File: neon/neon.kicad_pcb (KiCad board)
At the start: 2 copper layers, 60 x 50 mm, 32 parts, among them J1 V3V3-VIO, J2 3xV3V3-GND, J5 VBUS-VCC, U1 FT4232H_module, U2 C, U3 B, U4 A, U5 D, U6 74HC595

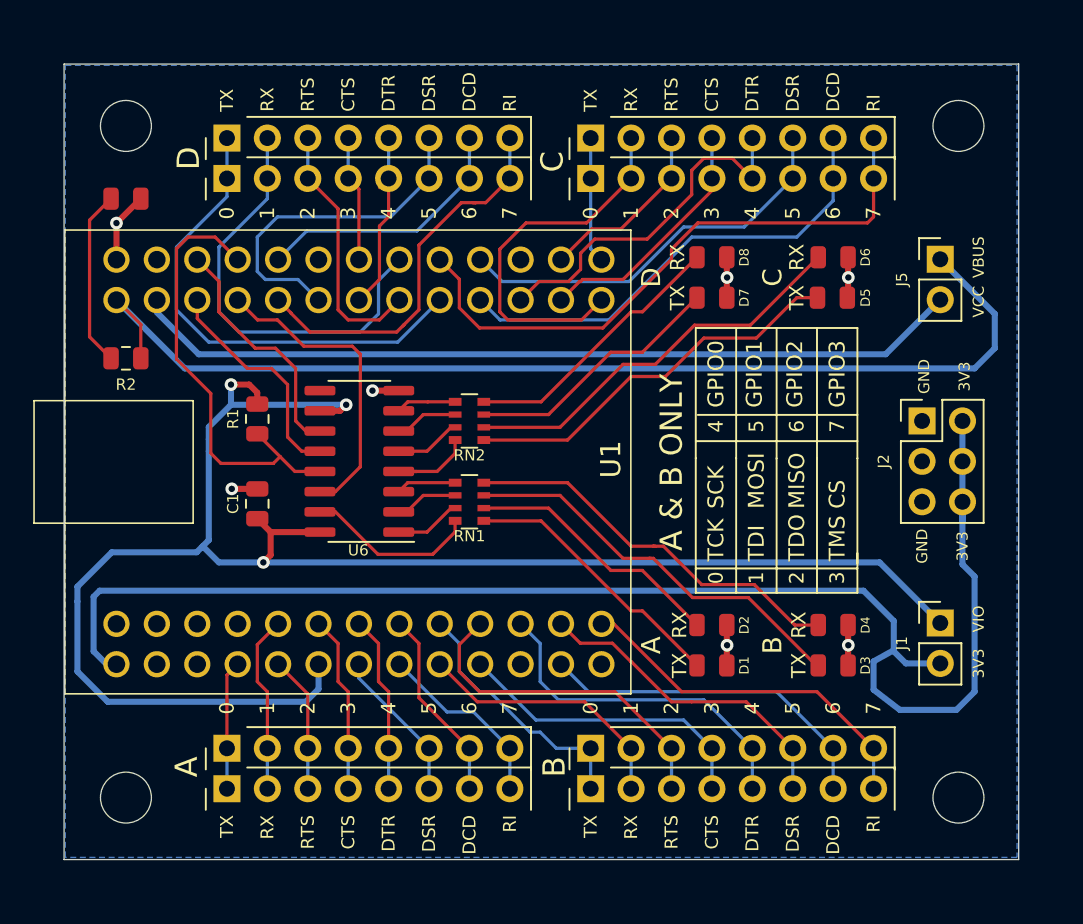
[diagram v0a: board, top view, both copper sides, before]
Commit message: Minor modifications following data review
Updated with updated copper pour, rounded edges. descrete resistors
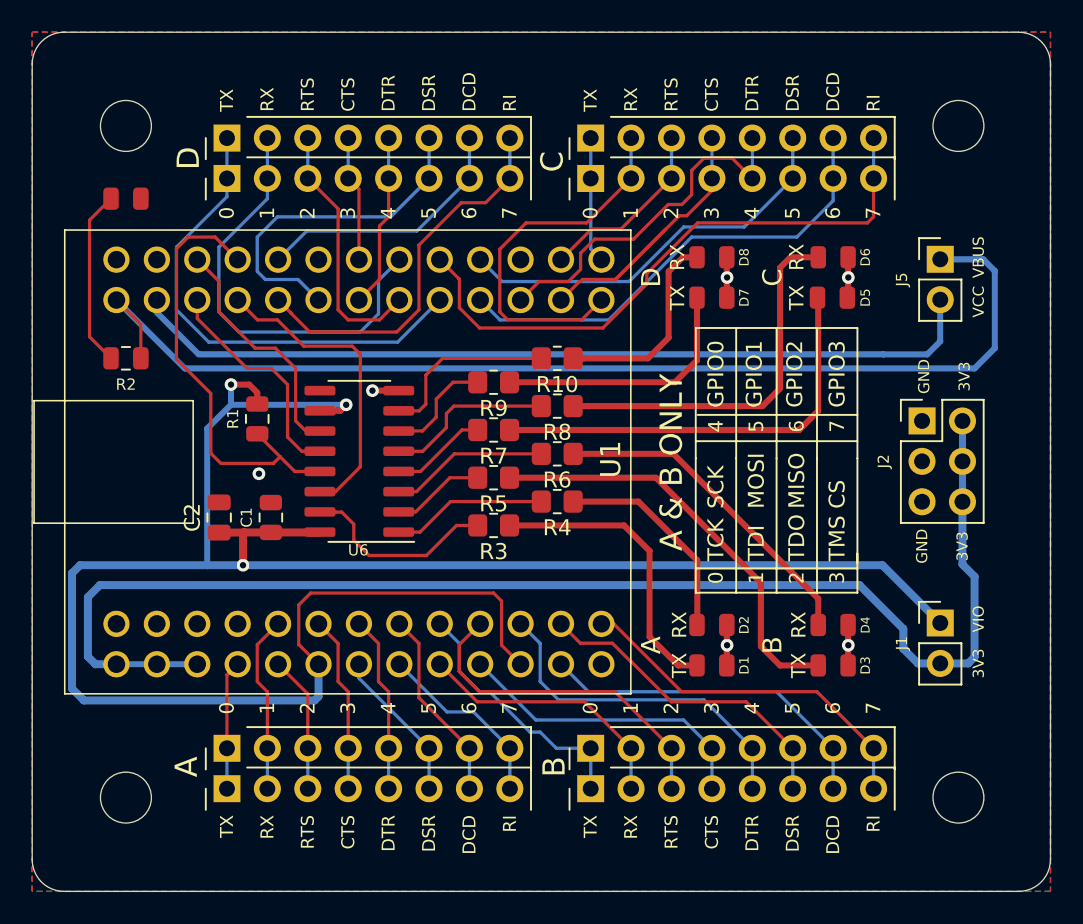
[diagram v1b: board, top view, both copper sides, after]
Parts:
- removed RN1, RN2: 330, Resistor_SMD:R_Array_Convex_4x0603
- added C2: 1uF, Capacitor_SMD:C_0805_2012Metric, F.Cu at (125.2, 108.4)
- added G***: LOGO, neon_footprints:sdg30pcbnew, B.Cu at (159.2, 104.9)
- added R10: 300R, Resistor_SMD:R_0805_2012Metric_Pad1.20x1.40mm_HandSolder, F.Cu at (146.5, 98.4)
- added R3: 300R, Resistor_SMD:R_0805_2012Metric_Pad1.20x1.40mm_HandSolder, F.Cu at (142.5, 108.9)
- added R4: 300R, Resistor_SMD:R_0805_2012Metric_Pad1.20x1.40mm_HandSolder, F.Cu at (146.5, 107.4)
- added R5: 300R, Resistor_SMD:R_0805_2012Metric_Pad1.20x1.40mm_HandSolder, F.Cu at (142.5, 105.9)
- added R6: 300R, Resistor_SMD:R_0805_2012Metric_Pad1.20x1.40mm_HandSolder, F.Cu at (146.5, 104.4)
- added R7: 300R, Resistor_SMD:R_0805_2012Metric_Pad1.20x1.40mm_HandSolder, F.Cu at (142.5, 102.9)
- added R8: 300R, Resistor_SMD:R_0805_2012Metric_Pad1.20x1.40mm_HandSolder, F.Cu at (146.5, 101.4)
- added R9: 300R, Resistor_SMD:R_0805_2012Metric_Pad1.20x1.40mm_HandSolder, F.Cu at (142.5, 99.9)
- R2: value 100 -> 300R
- moved G*** 15.4 mm to (143.2, 104.9)
- moved C1 1.21 mm to (128.5, 108.4)
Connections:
- net /FT4232H.sch/AD0 renamed /AD0
- net /FT4232H.sch/AD1 renamed /AD1
- net /FT4232H.sch/AD2 renamed /AD2
- net /FT4232H.sch/AD3 renamed /AD3
- net /FT4232H.sch/AD4 renamed /AD4
- net /FT4232H.sch/AD5 renamed /AD5
- net /FT4232H.sch/AD6 renamed /AD6
- net /FT4232H.sch/AD7 renamed /AD7
- net /FT4232H.sch/BD0 renamed /BD0
- net /FT4232H.sch/BD1 renamed /BD1
- net /FT4232H.sch/BD2 renamed /BD2
- net /FT4232H.sch/BD3 renamed /BD3
- net /FT4232H.sch/BD4 renamed /BD4
- net /FT4232H.sch/BD5 renamed /BD5
- net /FT4232H.sch/BD6 renamed /BD6
- net /FT4232H.sch/BD7 renamed /BD7
- net /FT4232H.sch/CD0 renamed /CD0
- net /FT4232H.sch/CD1 renamed /CD1
- net /FT4232H.sch/CD2 renamed /CD2
- net /FT4232H.sch/CD3 renamed /CD3
- net /FT4232H.sch/CD4 renamed /CD4
- net /FT4232H.sch/CD5 renamed /CD5
- net /FT4232H.sch/CD6 renamed /CD6
- net /FT4232H.sch/CD7 renamed /CD7
- net /FT4232H.sch/CLK renamed /CLK
- net /FT4232H.sch/CS renamed /CS
- net /FT4232H.sch/DATA renamed /DATA
- net /FT4232H.sch/DD0 renamed /DD0
- net /FT4232H.sch/DD1 renamed /DD1
- net /FT4232H.sch/DD2 renamed /DD2
- net /FT4232H.sch/DD3 renamed /DD3
- net /FT4232H.sch/DD4 renamed /DD4
- net /FT4232H.sch/DD5 renamed /DD5
- net /FT4232H.sch/DD6 renamed /DD6
- net /FT4232H.sch/DD7 renamed /DD7
- net /FT4232H.sch/PWREN renamed /PWREN
- net /FT4232H.sch/VBUS renamed /VBUS
- net /FT4232H.sch/VCC renamed /VCC
- C1 pad 1: /FT4232H.sch/VIO -> /VIO
- J1 pad 1: /FT4232H.sch/VIO -> /VIO
- R1 pad 2: /FT4232H.sch/VIO -> /VIO
- U1 pad 11: (no net) -> /VIO
- U1 pad 13: (no net) -> no_connect_59
- U1 pad 14: (no net) -> GND
- U1 pad 15: (no net) -> GND
- U1 pad 16: (no net) -> GND
- U1 pad 17: (no net) -> no_connect_60
- U1 pad 2: (no net) -> V3V3
- U1 pad 3: (no net) -> V3V3
- U1 pad 41: (no net) -> GND
- U1 pad 45: (no net) -> no_connect_61
- U1 pad 50: (no net) -> no_connect_62
- U1 pad 6: /FT4232H.sch/VIO -> /VIO
- U6 pad 10: /FT4232H.sch/VIO -> /VIO
- U6 pad 16: /FT4232H.sch/VIO -> /VIO
- U6 pad 9: (no net) -> no_connect_63
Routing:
- net /VIO: track 0.00 -> 135.5 mm, vias 0 -> 3
- net /FT4232H.sch/VIO: track 109.3 -> 0.00 mm, vias 3 -> 0
- net Net-(R10-Pad2): track 3.78 -> 11.4 mm
- net Net-(R6-Pad2): track 3.78 -> 9.95 mm
- net GND: track 17.9 -> 11.8 mm, vias 7 -> 6
- net Net-(R8-Pad2): track 4.68 -> 10.7 mm
- net Net-(R4-Pad2): track 4.68 -> 9.76 mm
- net /CD3: track 15.8 -> 20.1 mm
- net Net-(D4-Pad2): track 24.7 -> 20.8 mm
- net Net-(D8-Pad2): track 17.2 -> 13.5 mm
- net Net-(D2-Pad2): track 16.4 -> 13.4 mm
- net Net-(R9-Pad2): track 4.18 -> 6.90 mm
- net Net-(R3-Pad2): track 10.9 -> 13.4 mm
- net Net-(D5-Pad2): track 24.7 -> 27.0 mm
- net Net-(D6-Pad2): track 25.4 -> 23.7 mm
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- added copper zone on F.Cu, net GND
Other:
- board size 60 x 50 mm -> 64 x 54 mm
- net class Default removed
- net class grubasek removed
- net class zasilanko removed
